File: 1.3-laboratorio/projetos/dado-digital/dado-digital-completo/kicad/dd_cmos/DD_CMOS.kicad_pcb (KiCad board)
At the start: 2 copper layers, 50.8 x 50.8 mm, 10 parts, among them J1 Conn_01x02, J2 Conn_01x02, J4 Conn_01x01, J5 Conn_01x02, Q1 BC547

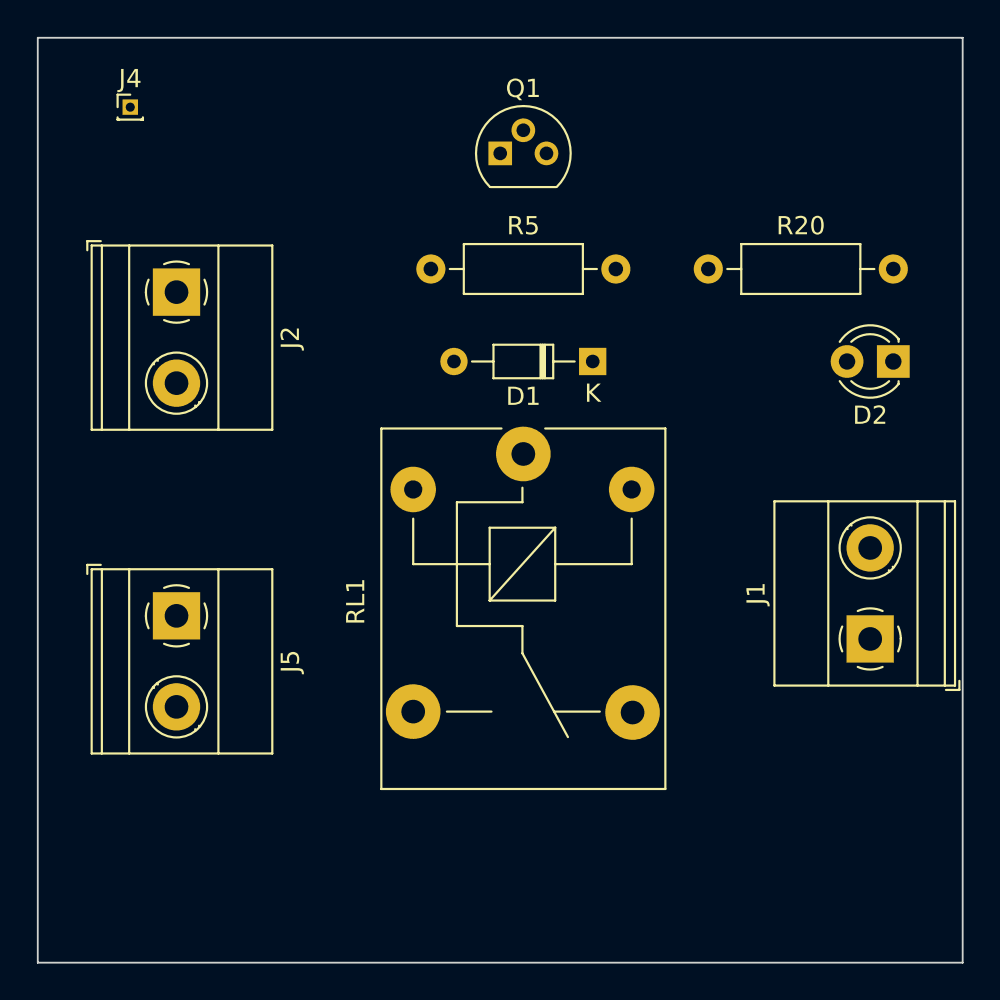
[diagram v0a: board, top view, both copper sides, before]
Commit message: Concluído o leiaute da PCI do módulo 'Atuador e Carga' do Dado Digital Completo. Falta fazer a revisão final e solicitar o orçamento.
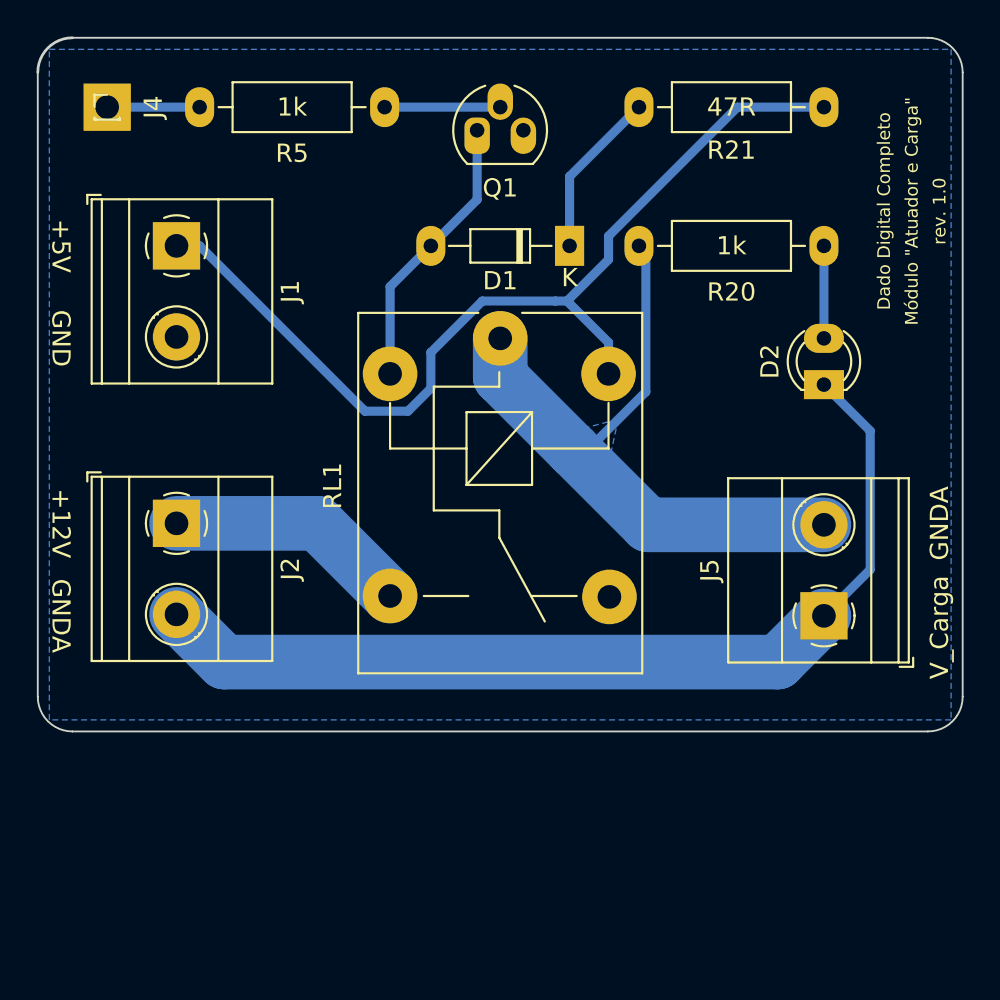
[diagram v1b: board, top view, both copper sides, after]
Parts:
- added R21: 47R, Resistor_THT:R_Axial_DIN0207_L6.3mm_D2.5mm_P10.16mm_Horizontal, F.Cu at (144.8, 90.2)
- Q1: footprint Package_TO_SOT_THT:TO-92 -> Package_TO_SOT_THT:TO-92_HandSolder
- RL1: value FINDER-40.51 -> HF3FA/005-ZSTF
- moved J1 43.8 mm to (109.2, 97.8), turned to 270 degrees
- moved J5 35.6 mm to (144.8, 118.1), turned to 90 degrees
- moved R5 15.5 mm to (110.5, 90.2)
- moved J2 12.7 mm to (109.2, 113.0)
- moved D1 6.48 mm to (130.8, 97.8)
- moved RL1 6.48 mm to (127.0, 102.9)
- moved D2 4.02 mm to (144.8, 105.4), turned to 90 degrees
- moved R20 4.02 mm to (134.6, 97.8)
- moved Q1 1.80 mm to (125.7, 91.4)
- moved J4 1.27 mm to (105.4, 90.2)
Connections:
- D1 pad 1: VDD -> Net-(D1-Pad1)
- D2 pad 1: GND -> Earth
- J1 pad 1: GND -> VDD
- J1 pad 2: VDD -> GND
- J2 pad 1: Earth -> +12V
- J2 pad 2: +12V -> Earth
- J5 pad 1: Net-(J5-Pad1) -> Earth
- J5 pad 2: Earth -> Net-(J5-Pad2)
- R20 pad 1: Net-(J5-Pad1) -> Net-(J5-Pad2)
- RL1 pad 11: Net-(J5-Pad1) -> Net-(J5-Pad2)
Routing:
- net VDD: track 0.00 -> 53.1 mm
- net Earth: track 0.00 -> 52.5 mm
- net Net-(J5-Pad2): track 0.00 -> 36.7 mm
- net Net-(D1-Pad2): track 0.00 -> 15.4 mm
- net +12V: track 0.00 -> 13.4 mm
- net Net-(D1-Pad1): track 0.00 -> 9.20 mm
- net Net-(Q1-Pad2): track 0.00 -> 6.35 mm
- net Net-(J4-Pad1): track 0.00 -> 5.08 mm
- net Net-(D2-Pad2): track 0.00 -> 5.08 mm
- net GND: track 0.00 -> 0.64 mm
- added copper zone on B.Cu, net GND
- added copper zone on B.Cu, net Net-(J5-Pad2)
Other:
- board size 50.8 x 50.8 mm -> 50.8 x 38.1 mm
- net class Default: clearance 0.2 -> 0.3; trace_width 0.25 -> 0.5; via_dia 0.8 -> 1.2; via_drill 0.4 -> 0.6
- net class GND added: clearance 0.3, trace_width 0.5, via_dia 1.2, via_drill 0.6
- net class Vcc added: clearance 0.3, trace_width 0.5, via_dia 1.2, via_drill 0.6
- rule trace_clearance: 0.2 -> 0.3
- rule trace_min: 0.2 -> 0.3
- board text added: "+12V"
- board text added: "+5V"
- board text added: "Dado Digital Completo"
- board text added: "GND"
- board text added: "GNDA"
- board text added: "Módulo "Atuador e Carga""
- board text added: "V_Carga"
- board text added: "rev. 1.0"
